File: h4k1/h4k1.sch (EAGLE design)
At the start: 198 parts, among them IC1 STM32F10XCXT6, J2 PJ-313D-AUDIO-JACK, J3 USB-AF10, K1 CHERRY-MX-LED, K10 CHERRY-MX, K11 CHERRY-MX, K12 CHERRY-MX, K13 CHERRY-MX, K14 CHERRY-MX, K15 CHERRY-MX, K16 CHERRY-MX, K17 CHERRY-MX-LED, K18 CHERRY-MX, K19 CHERRY-MX, K2 CHERRY-MX-LED, K20 CHERRY-MX, K21 CHERRY-MX, K22 CHERRY-MX, K23 CHERRY-MX, K24 CHERRY-MX, K25 CHERRY-MX-LED, K26 CHERRY-MX, K27 CHERRY-MX, K28 CHERRY-MX, K29 CHERRY-MX, K3 CHERRY-MX-LED, K30 CHERRY-MX, K31 CHERRY-MX, K32 CHERRY-MX, K33 CHERRY-MX-LED, K34 CHERRY-MX, K35 CHERRY-MX, K36 CHERRY-MX-LED, K37 CHERRY-MX-LED, K38 CHERRY-MX, K39 CHERRY-MX, K4 CHERRY-MX-LED, K40 CHERRY-MX-LED, K41 CHERRY-MX, K42 CHERRY-MX, K43 CHERRY-MX, K44 CHERRY-MX, K45 CHERRY-MX, K46 CHERRY-MX-LED, K5 CHERRY-MX-LED, K6 CHERRY-MX-LED, K65 EVQPUL02K, K66 EVQPUL02K, K67 K3-1280S-F2, K7 CHERRY-MX-LED, K8 CHERRY-MX-LED, K9 CHERRY-MX-LED, T1 DBG, U1 GL850G, U3 PCM2704CDB, X3 12MHz, X4 12MHz

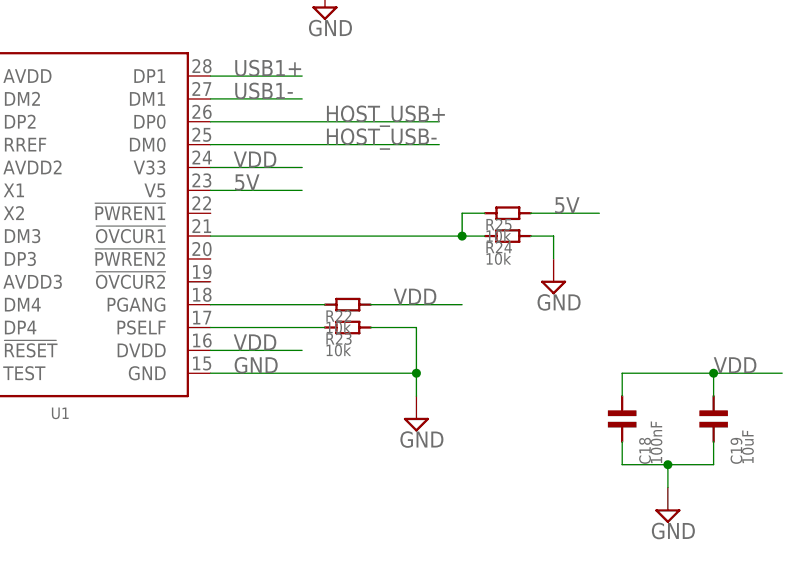
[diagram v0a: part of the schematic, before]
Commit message: update keybord for gl850 not limit power usage
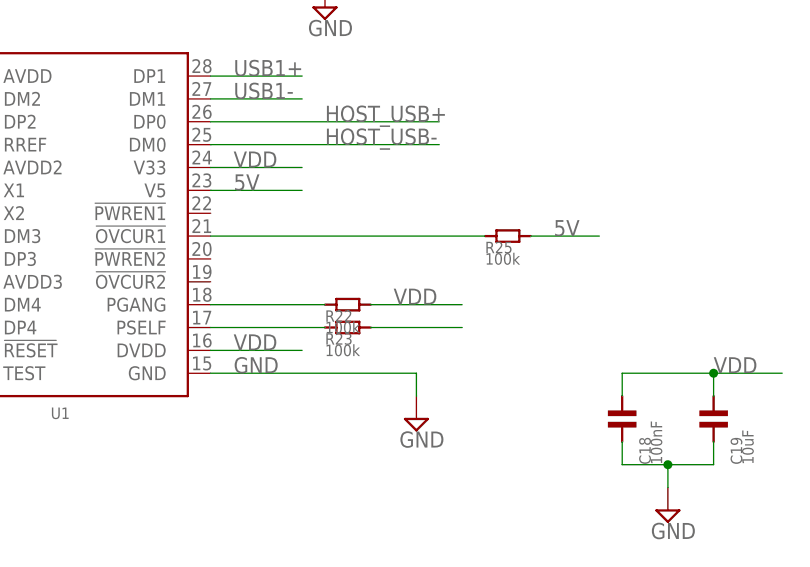
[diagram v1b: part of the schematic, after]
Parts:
- removed R24: 10k, hqc:R-0805
- R22, R23, R25: value 10k -> 100k
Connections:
- net 5V: now also R23.P$2
- net GND: no longer R23.P$2, R24.P$2
- net N$34: no longer R24.P$1
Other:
- moved on the sheet: R25
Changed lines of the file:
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@@
 <part name="SUPPLY13" library="supply2" deviceset="GND" device=""/>
 <part name="SUPPLY14" library="supply2" deviceset="GND" device=""/>
-<part name="R22" library="hqc" deviceset="R-0805" device="" value="10k"/>
-<part name="R23" library="hqc" deviceset="R-0805" device="" value="10k"/>
-<part name="R24" library="hqc" deviceset="R-0805" device="" value="10k"/>
-<part name="R25" library="hqc" deviceset="R-0805" device="" value="10k"/>
-<part name="SUPPLY15" library="supply2" deviceset="GND" device=""/>
+<part name="R22" library="hqc" deviceset="R-0805" device="" value="100k"/>
+<part name="R23" library="hqc" deviceset="R-0805" device="" value="100k"/>
+<part name="R25" library="hqc" deviceset="R-0805" device="" value="100k"/>
 <part name="J1" library="hqc-connector" deviceset="PH-5AWD" device=""/>
 <part name="U3" library="hqc" deviceset="PCM2704CDB" device=""/>
@@
 <instance part="R22" gate="G$1" x="91.44" y="198.12"/>
 <instance part="R23" gate="G$1" x="91.44" y="195.58"/>
-<instance part="R24" gate="G$1" x="109.22" y="205.74"/>
-<instance part="R25" gate="G$1" x="109.22" y="208.28"/>
-<instance part="SUPPLY15" gate="GND" x="114.3" y="200.66"/>
+<instance part="R25" gate="G$1" x="109.22" y="205.74"/>
 <instance part="J1" gate="G$1" x="-43.18" y="264.16"/>
 <instance part="U3" gate="PCM2704CDB" x="266.7" y="226.06"/>
@@
 <pinref part="SUPPLY14" gate="GND" pin="GND"/>
 <wire x1="99.06" y1="190.5" x2="99.06" y2="187.96" width="0.1524" layer="91"/>
-<pinref part="R23" gate="G$1" pin="P$2"/>
-<wire x1="93.98" y1="195.58" x2="99.06" y2="195.58" width="0.1524" layer="91"/>
-<wire x1="99.06" y1="195.58" x2="99.06" y2="190.5" width="0.1524" layer="91"/>
-<junction x="99.06" y="190.5"/>
 </segment>
 <segment>
@@
 <wire x1="127" y1="180.34" x2="127" y2="177.8" width="0.1524" layer="91"/>
 <junction x="127" y="180.34"/>
-</segment>
-<segment>
-<pinref part="R24" gate="G$1" pin="P$2"/>
-<wire x1="111.76" y1="205.74" x2="114.3" y2="205.74" width="0.1524" layer="91"/>
-<pinref part="SUPPLY15" gate="GND" pin="GND"/>
-<wire x1="114.3" y1="205.74" x2="114.3" y2="203.2" width="0.1524" layer="91"/>
 </segment>
 <segment>
@@
 <segment>
 <pinref part="R25" gate="G$1" pin="P$2"/>
-<wire x1="111.76" y1="208.28" x2="119.38" y2="208.28" width="0.1524" layer="91"/>
-<label x="114.3" y="208.28" size="1.778" layer="95"/>
+<wire x1="111.76" y1="205.74" x2="119.38" y2="205.74" width="0.1524" layer="91"/>
+<label x="114.3" y="205.74" size="1.778" layer="95"/>
+</segment>
+<segment>
+<pinref part="R23" gate="G$1" pin="P$2"/>
+<wire x1="93.98" y1="195.58" x2="104.14" y2="195.58" width="0.1524" layer="91"/>
 </segment>
 </net>
@@
 <segment>
 <pinref part="U1" gate="GL850G" pin="!OVCUR1"/>
-<pinref part="R24" gate="G$1" pin="P$1"/>
-<wire x1="76.2" y1="205.74" x2="104.14" y2="205.74" width="0.1524" layer="91"/>
-<wire x1="104.14" y1="205.74" x2="106.68" y2="205.74" width="0.1524" layer="91"/>
-<wire x1="104.14" y1="205.74" x2="104.14" y2="208.28" width="0.1524" layer="91"/>
-<junction x="104.14" y="205.74"/>
+<wire x1="76.2" y1="205.74" x2="106.68" y2="205.74" width="0.1524" layer="91"/>
 <pinref part="R25" gate="G$1" pin="P$1"/>
-<wire x1="104.14" y1="208.28" x2="106.68" y2="208.28" width="0.1524" layer="91"/>
-</segment>
-</net>
+</segment>
+</net>

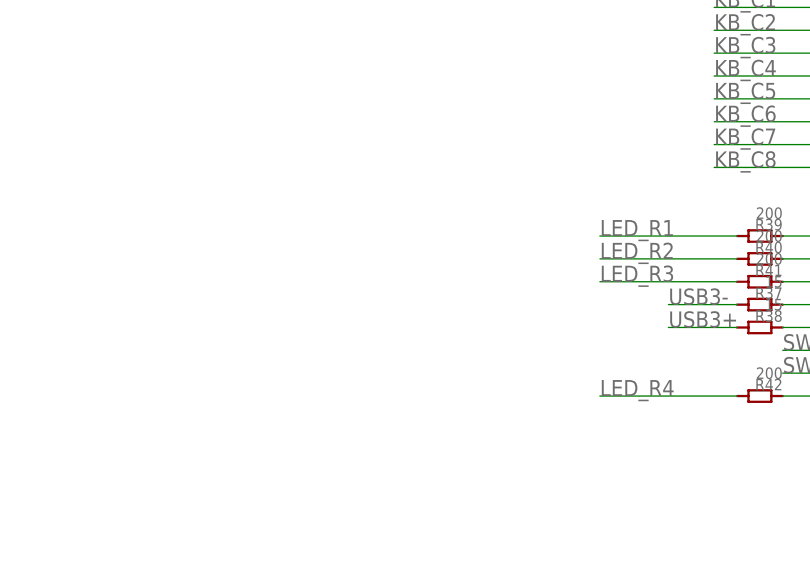
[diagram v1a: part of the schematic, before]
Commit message: add usb pull up resistor
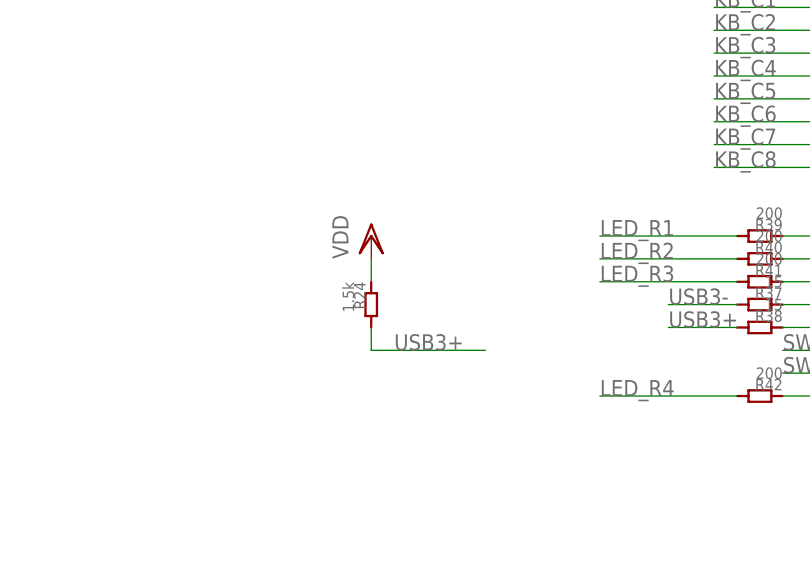
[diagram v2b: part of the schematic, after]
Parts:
- added R24: 1.5k, hqc:R-0805
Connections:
- net USB3+: now also R24.P$2
- net VDD: now also R24.P$1
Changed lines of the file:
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@@
 <part name="U$7" library="hqc" deviceset="M2-MOUNTING-HOLE" device=""/>
 <part name="U$8" library="hqc" deviceset="M2-MOUNTING-HOLE" device=""/>
+<part name="VDD18" library="supply1" deviceset="VDD" device=""/>
+<part name="R24" library="hqc" deviceset="R-0805" device="" value="1.5k"/>
 </parts>
 <sheets>
@@
 <instance part="U$7" gate="G$1" x="647.7" y="-127"/>
 <instance part="U$8" gate="G$1" x="627.38" y="-127"/>
+<instance part="VDD18" gate="G$1" x="-12.7" y="45.72"/>
+<instance part="R24" gate="G$1" x="-12.7" y="38.1" rot="R270"/>
 </instances>
 <busses>
@@
 <wire x1="78.74" y1="101.6" x2="78.74" y2="104.14" width="0.1524" layer="91"/>
 </segment>
+<segment>
+<pinref part="VDD18" gate="G$1" pin="VDD"/>
+<pinref part="R24" gate="G$1" pin="P$1"/>
+<wire x1="-12.7" y1="43.18" x2="-12.7" y2="40.64" width="0.1524" layer="91"/>
+</segment>
 </net>
 <net name="KB_C1" class="0">
@@
 <label x="20.32" y="35.56" size="1.778" layer="95"/>
 </segment>
-</net>
+<segment>
+<pinref part="R24" gate="G$1" pin="P$2"/>
+<wire x1="-12.7" y1="35.56" x2="-12.7" y2="33.02" width="0.1524" layer="91"/>
+<wire x1="-12.7" y1="33.02" x2="0" y2="33.02" width="0.1524" layer="91"/>
+<label x="-10.16" y="33.02" size="1.778" layer="95"/>
+</segment>
+</net>

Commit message: using hqc bmx055
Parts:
- U$4: device sensor:BMX055 -> hqc:BMX055
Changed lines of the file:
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@@
 <part name="J3" library="hqc" deviceset="USB-AF10" device=""/>
 <part name="SUPPLY27" library="supply2" deviceset="GND" device=""/>
-<part name="U$4" library="sensor" deviceset="BMX055" device=""/>
+<part name="U$4" library="hqc" deviceset="BMX055" device=""/>
 <part name="VDD12" library="supply1" deviceset="VDD" device=""/>
 <part name="SUPPLY28" library="supply2" deviceset="GND" device=""/>

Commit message: update circuit
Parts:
- added U4: 74HC138, hqc:74HC138
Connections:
- new net MCU_RX: IC1PORTB_L.PB7
- new net MCU_TX: IC1PORTB_L.PB6
- new net RS_A0: IC1PORTB_L.PB1, U4.A0
- new net RS_A1: IC1PORTB_L.PB2, U4.A1
- new net RS_A2: IC1PORTB_L.PB3, U4.A2
- new net RS_EN: IC1PORTB_L.PB0, U4.E3
- net GND: now also U4.!E1, U4.!E2, U4.GND
- net KB_R1: now also U4.!Y0; no longer IC1PORTB_L.PB0
- net KB_R2: now also U4.!Y1; no longer IC1PORTB_L.PB1
- net KB_R3: now also U4.!Y2; no longer IC1PORTB_L.PB2
- net KB_R4: now also U4.!Y3; no longer IC1PORTB_L.PB3
- net KB_R5: now also U4.!Y4; no longer IC1PORTB_L.PB4
- net KB_R6: now also U4.!Y5; no longer IC1PORTB_L.PB5
- net KB_R7: now also U4.!Y6; no longer IC1PORTB_L.PB6
- net N$76: now also IC1PORTB_L.PB4; no longer IC1PORTA_H.PA8
- net N$80: now also IC1PORTB_L.PB5; no longer IC1PORTA_H.PA9
- net N$81: now also IC1PORTB_H.PB15, R42.P$1; no longer IC1PORTA_H.PA10, R41.P$1
- net N$85: now also IC1PORTB_H.PB14, R41.P$1; no longer IC1PORTA_H.PA15, R42.P$1
- net VDD: now also U4.VCC
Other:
- moved on the sheet: IC1PORTA_H, IC1PORTA_L, IC1PORTB_H, IC1PORTB_L, R37, R38, R39, R40, R41, R42, T1

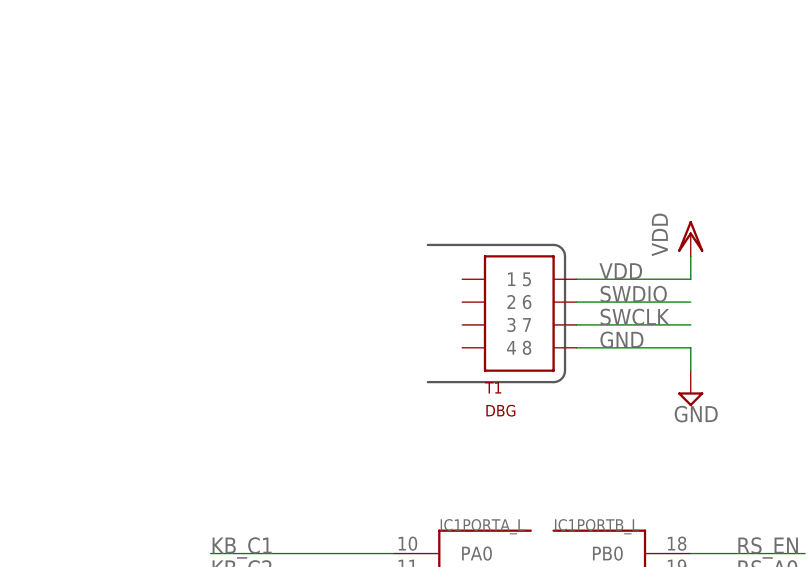
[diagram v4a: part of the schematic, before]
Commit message: add serial port
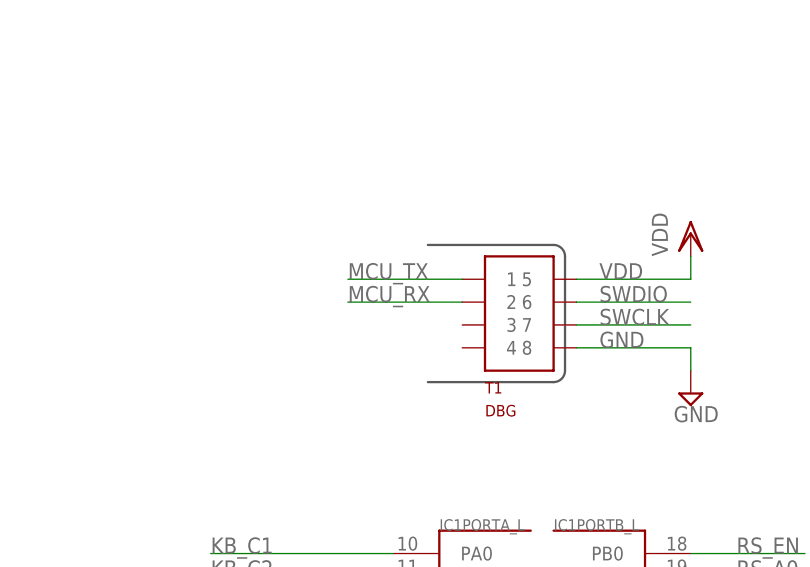
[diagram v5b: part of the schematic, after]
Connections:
- net MCU_RX: now also T1.2
- net MCU_TX: now also T1.1
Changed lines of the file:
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@@
 <setting verticaltext="up"/>
 </settings>
-<grid distance="0.1" unitdist="inch" unit="inch" style="lines" multiple="1" display="yes" altdistance="0.01" altunitdist="inch" altunit="inch"/>
+<grid distance="0.1" unitdist="inch" unit="inch" style="lines" multiple="1" display="no" altdistance="0.01" altunitdist="inch" altunit="inch"/>
 <layers>
 <layer number="1" name="Top" color="4" fill="1" visible="no" active="no"/>
@@
 <label x="73.66" y="55.88" size="1.778" layer="95"/>
 </segment>
+<segment>
+<pinref part="T1" gate="G$1" pin="1"/>
+<wire x1="45.72" y1="101.6" x2="33.02" y2="101.6" width="0.1524" layer="91"/>
+<label x="33.02" y="101.6" size="1.778" layer="95"/>
+</segment>
 </net>
 <net name="MCU_RX" class="0">
@@
 <label x="73.66" y="53.34" size="1.778" layer="95"/>
 </segment>
+<segment>
+<pinref part="T1" gate="G$1" pin="2"/>
+<wire x1="45.72" y1="99.06" x2="33.02" y2="99.06" width="0.1524" layer="91"/>
+<label x="33.02" y="99.06" size="1.778" layer="95"/>
+</segment>
 </net>

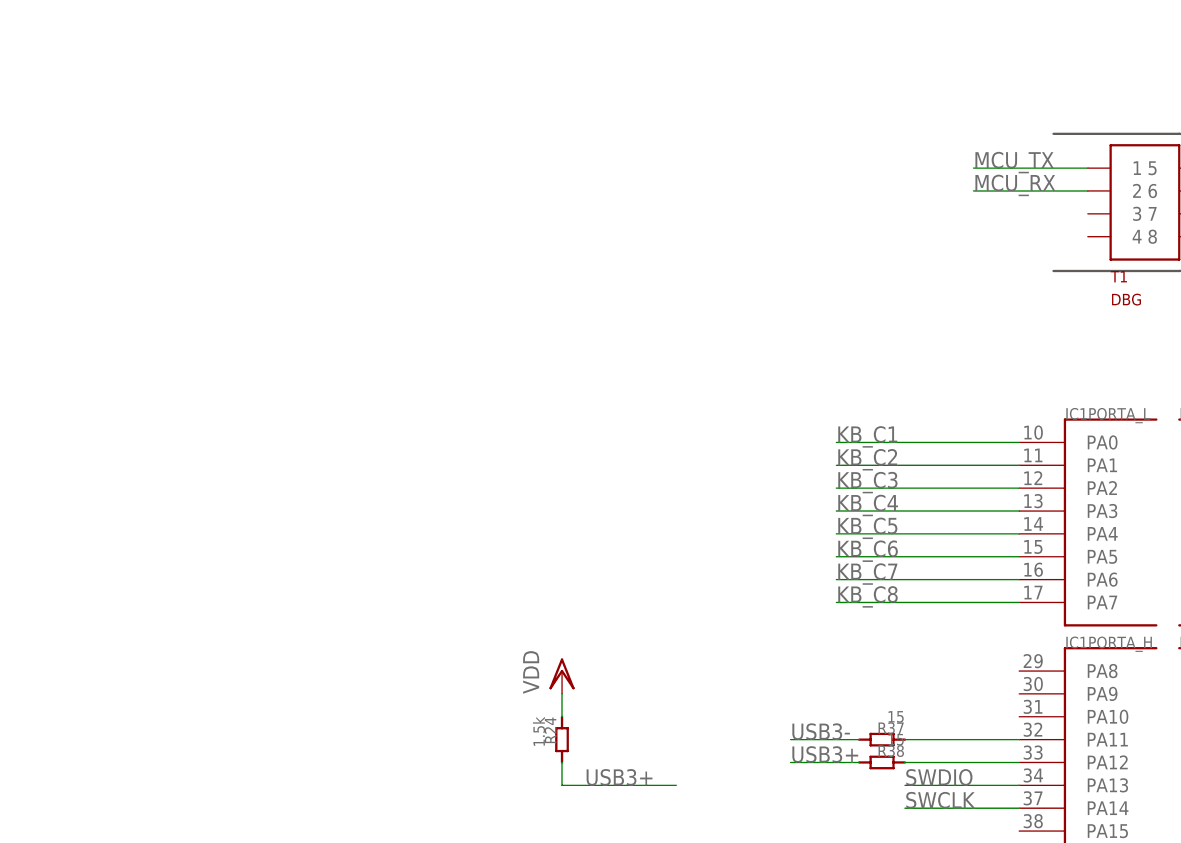
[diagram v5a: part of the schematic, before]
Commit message: add vbus sense circuit
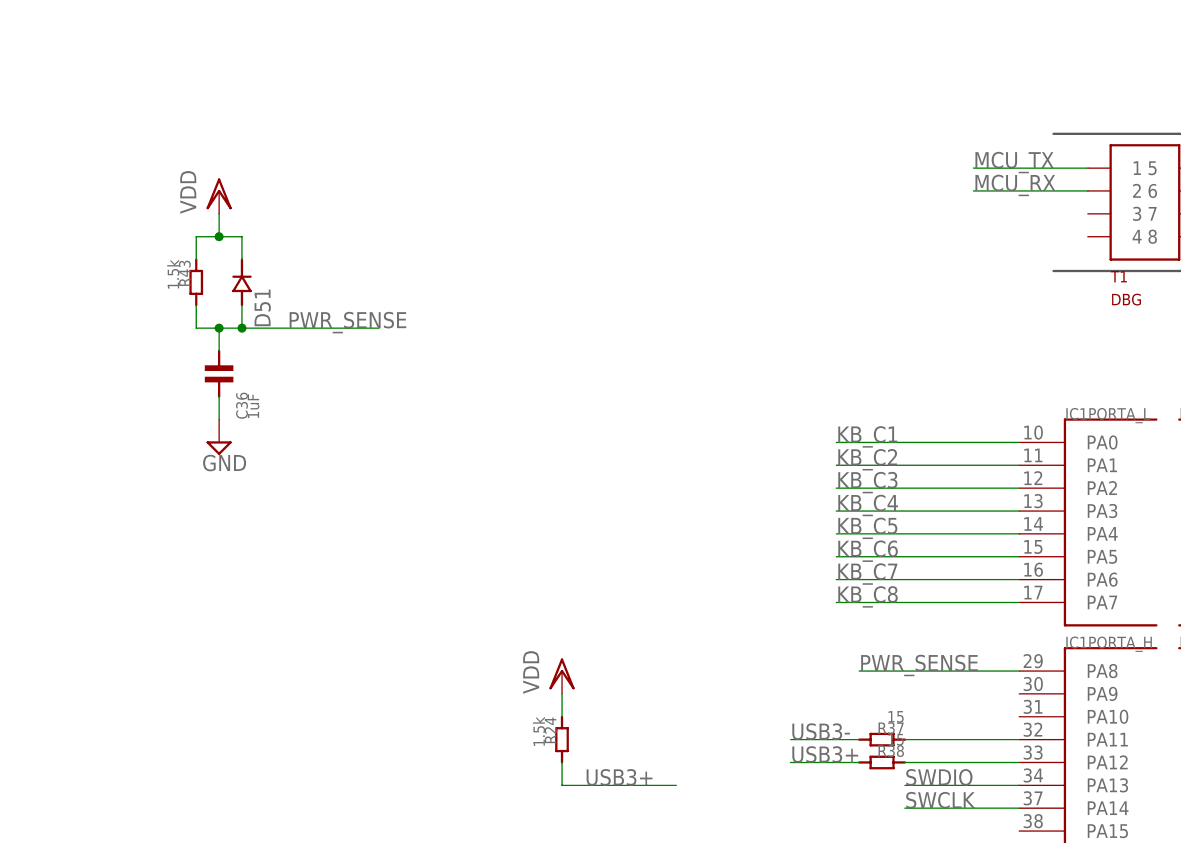
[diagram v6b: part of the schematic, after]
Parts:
- added C36: 1uF, hqc:C-0805
- added D51: (no value), hqc-basic:IN4148WS-SWITCHING-DIODE
- added R43: 1.5k, hqc:R-0805
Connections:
- new net PWR_SENSE: C36.P$2, D51.P$1, IC1PORTA_H.PA8, R43.P$2
- net GND: now also C36.P$1
- net VDD: now also D51.P$2, R43.P$1
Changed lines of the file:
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@@
 <setting verticaltext="up"/>
 </settings>
-<grid distance="0.1" unitdist="inch" unit="inch" style="lines" multiple="1" display="no" altdistance="0.01" altunitdist="inch" altunit="inch"/>
+<grid distance="0.1" unitdist="inch" unit="inch" style="lines" multiple="1" display="yes" altdistance="0.01" altunitdist="inch" altunit="inch"/>
 <layers>
 <layer number="1" name="Top" color="4" fill="1" visible="no" active="no"/>
@@
 <part name="VDD19" library="supply1" deviceset="VDD" device=""/>
 <part name="SUPPLY15" library="supply2" deviceset="GND" device=""/>
+<part name="VDD20" library="supply1" deviceset="VDD" device=""/>
+<part name="R43" library="hqc" deviceset="R-0805" device="" value="1.5k"/>
+<part name="C36" library="hqc" deviceset="C-0805" device="" value="1uF"/>
+<part name="SUPPLY32" library="supply2" deviceset="GND" device=""/>
+<part name="D51" library="hqc-basic" deviceset="IN4148WS-SWITCHING-DIODE" device=""/>
 </parts>
 <sheets>
@@
 <instance part="VDD19" gate="G$1" x="-63.5" y="-127"/>
 <instance part="SUPPLY15" gate="GND" x="-76.2" y="-167.64"/>
+<instance part="VDD20" gate="G$1" x="-50.8" y="99.06"/>
+<instance part="R43" gate="G$1" x="-53.34" y="88.9" rot="R270"/>
+<instance part="C36" gate="G$1" x="-50.8" y="78.74" rot="R90"/>
+<instance part="SUPPLY32" gate="GND" x="-50.8" y="71.12"/>
+<instance part="D51" gate="G$1" x="-48.26" y="88.9" rot="R90"/>
 </instances>
 <busses>
@@
 <wire x1="-63.5" y1="-134.62" x2="-63.5" y2="-129.54" width="0.1524" layer="91"/>
 </segment>
+<segment>
+<pinref part="VDD20" gate="G$1" pin="VDD"/>
+<wire x1="-50.8" y1="96.52" x2="-50.8" y2="93.98" width="0.1524" layer="91"/>
+<wire x1="-50.8" y1="93.98" x2="-53.34" y2="93.98" width="0.1524" layer="91"/>
+<pinref part="R43" gate="G$1" pin="P$1"/>
+<wire x1="-53.34" y1="93.98" x2="-53.34" y2="91.44" width="0.1524" layer="91"/>
+<wire x1="-50.8" y1="93.98" x2="-48.26" y2="93.98" width="0.1524" layer="91"/>
+<junction x="-50.8" y="93.98"/>
+<pinref part="D51" gate="G$1" pin="P$2"/>
+<wire x1="-48.26" y1="91.44" x2="-48.26" y2="93.98" width="0.1524" layer="91"/>
+</segment>
 </net>
 <net name="KB_C1" class="0">
@@
 <junction x="-76.2" y="-142.24"/>
 </segment>
+<segment>
+<pinref part="C36" gate="G$1" pin="P$1"/>
+<pinref part="SUPPLY32" gate="GND" pin="GND"/>
+<wire x1="-50.8" y1="76.2" x2="-50.8" y2="73.66" width="0.1524" layer="91"/>
+</segment>
 </net>
 <net name="OSC32_1" class="0">
@@
 </segment>
 </net>
+<net name="PWR_SENSE" class="0">
+<segment>
+<pinref part="D51" gate="G$1" pin="P$1"/>
+<wire x1="-48.26" y1="86.36" x2="-48.26" y2="83.82" width="0.1524" layer="91"/>
+<wire x1="-48.26" y1="83.82" x2="-50.8" y2="83.82" width="0.1524" layer="91"/>
+<pinref part="R43" gate="G$1" pin="P$2"/>
+<wire x1="-50.8" y1="83.82" x2="-53.34" y2="83.82" width="0.1524" layer="91"/>
+<wire x1="-53.34" y1="83.82" x2="-53.34" y2="86.36" width="0.1524" layer="91"/>
+<pinref part="C36" gate="G$1" pin="P$2"/>
+<wire x1="-50.8" y1="83.82" x2="-50.8" y2="81.28" width="0.1524" layer="91"/>
+<junction x="-50.8" y="83.82"/>
+<wire x1="-48.26" y1="83.82" x2="-33.02" y2="83.82" width="0.1524" layer="91"/>
+<junction x="-48.26" y="83.82"/>
+<label x="-43.18" y="83.82" size="1.778" layer="95"/>
+</segment>
+<segment>
+<pinref part="IC1" gate="PORTA_H" pin="PA8"/>
+<wire x1="38.1" y1="45.72" x2="20.32" y2="45.72" width="0.1524" layer="91"/>
+<label x="20.32" y="45.72" size="1.778" layer="95"/>
+</segment>
+</net>
